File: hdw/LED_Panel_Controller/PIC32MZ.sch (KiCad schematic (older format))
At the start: 3 parts

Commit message: lots of schematic progress
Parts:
- removed U?: PIC32MZ0512EFE064T-I_PT, Package_QFP:TQFP-64_10x10mm_P0.5mm, symbol Custom_Library:PIC32MZ0512EFE064T-I_PT
- added U?: PIC32MZ2048EFG100_IPF, Housings_QFP:TQFP-100_14x14mm_Pitch0.5mm, symbol Custom_Library:PIC32MZ2048EFG100_IPF
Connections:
- net labels added: FLASH_SPI_MISO, FLASH_SPI_MOSI, FLASH_SPI_SCK, SD_CARD_DET, SD_SPI_CS, SD_SPI_MISO, SD_SPI_MOSI, SD_SPI_SCK, WIFI_CHIP_EN, WIFI_IRQN, WIFI_SPI_MISO, WIFI_SPI_MOSI, WIFI_SPI_SCK, WIFI_WAKE, ~FLASH_SPI_CE1, ~WIFI_RESET, ~WIFI_SPI_SS
- net labels removed: PIC32MZ_POSC_EC_Enable
- wire segments 33 -> 41
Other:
- note added: "I2C5"
- note added: "ICSP2"
- note added: "POSC"
- note added: "REFCLK1"
- note added: "SOSC"
- moved on the sheet: R?

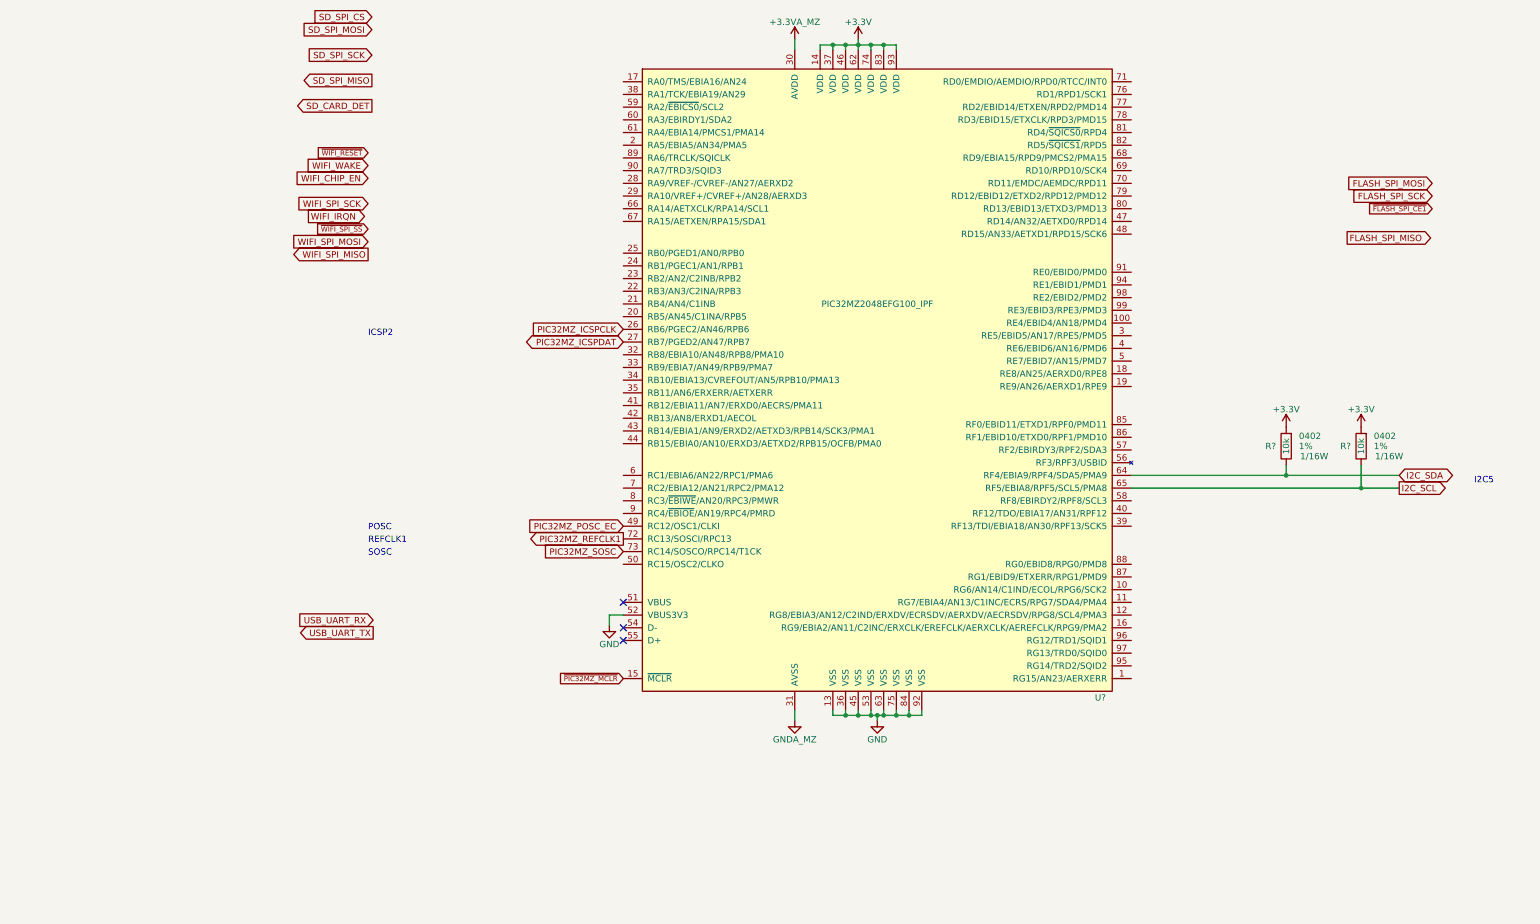
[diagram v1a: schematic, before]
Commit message: lots of MCU pin assignments
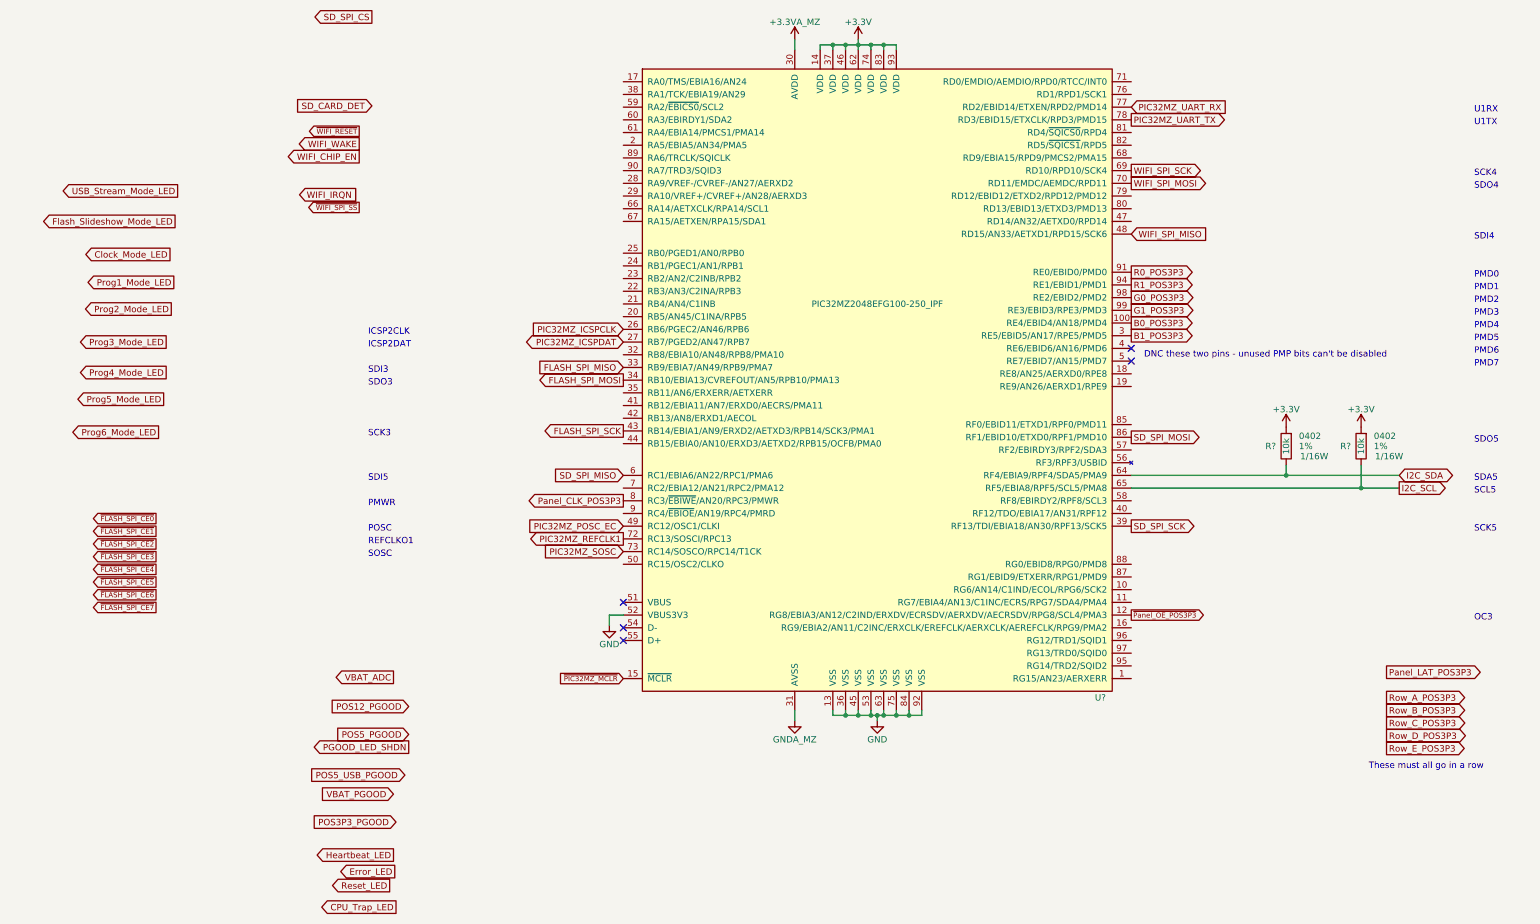
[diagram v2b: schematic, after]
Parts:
- U?: value PIC32MZ2048EFG100_IPF -> PIC32MZ2048EFG100-250_IPF; Digi-Key PN PIC32MZ2048EFG100-I/PF-ND -> PIC32MZ2048EFH100-250I/PF-ND
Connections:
- net FLASH_SPI_MISO: now also U?.33 (RB9/EBIA7/AN49/RPB9/PMA7)
- net FLASH_SPI_MOSI: now also U?.34 (RB10/EBIA13/CVREFOUT/AN5/RPB10/PMA13)
- net FLASH_SPI_SCK: now also U?.43 (RB14/EBIA1/AN9/ERXD2/AETXD3/RPB14/SCK3/PMA1)
- net SD_SPI_MISO: now also U?.6 (RC1/EBIA6/AN22/RPC1/PMA6)
- net SD_SPI_MOSI: now also U?.86 (RF1/EBID10/ETXD0/RPF1/PMD10)
- net SD_SPI_SCK: now also U?.39 (RF13/TDI/EBIA18/AN30/RPF13/SCK5)
- net WIFI_SPI_MISO: now also U?.48 (RD15/AN33/AETXD1/RPD15/SCK6)
- net WIFI_SPI_MOSI: now also U?.70 (RD11/EMDC/AEMDC/RPD11)
- net WIFI_SPI_SCK: now also U?.69 (RD10/RPD10/SCK4)
- net B0_POS3P3: now reaches U?.100 (RE4/EBID4/AN18/PMD4)
- net ~Panel_OE_POS3P3: now reaches U?.12 (RG8/EBIA3/AN12/C2IND/ERXDV/ECRSDV/AERXDV/AECRSDV/RPG8/SCL4/PMA3)
- net B1_POS3P3: now reaches U?.3 (RE5/EBID5/AN17/RPE5/PMD5)
- net PIC32MZ_UART_RX: now reaches U?.77 (RD2/EBID14/ETXEN/RPD2/PMD14)
- net PIC32MZ_UART_TX: now reaches U?.78 (RD3/EBID15/ETXCLK/RPD3/PMD15)
- net Panel_CLK_POS3P3: now reaches U?.8 (RC3/~EBIWE~/AN20/RPC3/PMWR)
- net R0_POS3P3: now reaches U?.91 (RE0/EBID0/PMD0)
- net R1_POS3P3: now reaches U?.94 (RE1/EBID1/PMD1)
- net G0_POS3P3: now reaches U?.98 (RE2/EBID2/PMD2)
- net G1_POS3P3: now reaches U?.99 (RE3/EBID3/RPE3/PMD3)
- no-connect marks 3 -> 5
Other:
- note added: "DNC these two pins - unused PMP bits can't be disabled"
- note added: "ICSP2CLK"
- note added: "ICSP2DAT"
- note added: "OC3"
- note added: "PMD0"
- note added: "PMD1"
- note added: "PMD2"
- note added: "PMD3"
- note added: "PMD4"
- note added: "PMD5"
- note added: "PMD6"
- note added: "PMD7"
- note added: "PMWR"
- note added: "REFCLKO1"
- note added: "SCK3"
- note added: "SCK4"
- note added: "SCK5"
- note added: "SCL5"
- note added: "SDA5"
- note added: "SDI3"
- note added: "SDI4"
- note added: "SDI5"
- note added: "SDO3"
- note added: "SDO4"
- note added: "SDO5"
- note added: "These must all go in a row"
- note added: "U1RX"
- note added: "U1TX"
- note removed: "I2C5"
- note removed: "ICSP2"
- note removed: "REFCLK1"
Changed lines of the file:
@@
 Text GLabel 3300 4890 0    50   Output ~ 0
 PIC32MZ_REFCLK1
-Text GLabel 1330 5630 0    50   Output ~ 0
-USB_UART_TX
-Text GLabel 1330 5530 0    50   Input ~ 0
-USB_UART_RX
+Text GLabel 7300 1590 2    50   Output ~ 0
+PIC32MZ_UART_TX
+Text GLabel 7300 1490 2    50   Input ~ 0
+PIC32MZ_UART_RX
 Text GLabel 3300 3240 0    50   Input ~ 0
 PIC32MZ_ICSPCLK
@@
 Text GLabel 3300 4990 0    50   Input ~ 0
 PIC32MZ_SOSC
-Text GLabel 1290 1850 0    40   Input ~ 0
+Text GLabel 1220 1680 0    40   Output ~ 0
 ~WIFI_RESET
-Text GLabel 1290 1950 0    50   Input ~ 0
+Text GLabel 1220 1780 0    50   Output ~ 0
 WIFI_WAKE
-Text GLabel 1290 2050 0    50   Input ~ 0
+Text GLabel 1220 1880 0    50   Output ~ 0
 WIFI_CHIP_EN
-Text GLabel 1290 2250 0    50   Input ~ 0
+Text GLabel 7300 1990 2    50   Output ~ 0
 WIFI_SPI_SCK
-Text GLabel 1290 2450 0    40   Input ~ 0
+Text GLabel 1220 2280 0    40   Output ~ 0
 ~WIFI_SPI_SS
-Text GLabel 1290 2550 0    50   Input ~ 0
+Text GLabel 7300 2090 2    50   Output ~ 0
 WIFI_SPI_MOSI
-Text GLabel 1290 2650 0    50   Output ~ 0
+Text GLabel 7300 2490 2    50   Input ~ 0
 WIFI_SPI_MISO
-Text GLabel 820  2350 2    50   Output ~ 0
+Text GLabel 750  2180 2    50   Input ~ 0
 WIFI_IRQN
 $Comp
@@
 P 5300 3640
 F 0 "U?" H 7100 1140 50  0000 R CNN
-F 1 "PIC32MZ2048EFG100_IPF" H 5300 4240 50  0000 C CNN
+F 1 "PIC32MZ2048EFG100-250_IPF" H 5300 4240 50  0000 C CNN
 F 2 "Housings_QFP:TQFP-100_14x14mm_Pitch0.5mm" H 5300 3640 50  0001 C CNN
 F 3 "http://ww1.microchip.com/downloads/en/DeviceDoc/60001320E.pdf" H 5300 3640 50  0001 C CNN
-F 4 "PIC32MZ2048EFG100-I/PF-ND" H 5300 3640 50  0001 C CNN "Digi-Key PN"
+F 4 "PIC32MZ2048EFH100-250I/PF-ND" H 5300 3640 50  0001 C CNN "Digi-Key PN"
 	1    5300 3640
 	1    0    0    -1
@@
 	1    0    0    -1
 $EndComp
-Text Notes 10000 4460 0    50   ~ 0
-I2C5
-Text Notes 1290 3300 0    50   ~ 0
-ICSP2
-Text Notes 1290 4830 0    50   ~ 0
+Text Notes 10000 4440 0    50   ~ 0
+SDA5
+Text Notes 1290 3290 0    50   ~ 0
+ICSP2CLK
+Text Notes 1290 4840 0    50   ~ 0
 POSC
-Text Notes 1290 4930 0    50   ~ 0
-REFCLK1
-Text Notes 1290 5030 0    50   ~ 0
+Text Notes 1290 4940 0    50   ~ 0
+REFCLKO1
+Text Notes 1290 5040 0    50   ~ 0
 SOSC
-Text GLabel 1320 780  0    50   Input ~ 0
+Text GLabel 1320 780  0    50   Output ~ 0
 SD_SPI_CS
-Text GLabel 1320 880  0    50   Input ~ 0
+Text GLabel 7300 4090 2    50   Output ~ 0
 SD_SPI_MOSI
-Text GLabel 1320 1080 0    50   Input ~ 0
+Text GLabel 7300 4790 2    50   Output ~ 0
 SD_SPI_SCK
-Text GLabel 1320 1280 0    50   Output ~ 0
+Text GLabel 3300 4390 0    50   Input ~ 0
 SD_SPI_MISO
-Text GLabel 1320 1480 0    50   Output ~ 0
+Text GLabel 1320 1480 0    50   Input ~ 0
 SD_CARD_DET
-Text GLabel 9670 2190 0    50   Input ~ 0
+Text GLabel 3300 4040 0    50   Output ~ 0
 FLASH_SPI_SCK
-Text GLabel 9670 2290 0    40   Input ~ 0
+Text GLabel 3300 3640 0    50   Output ~ 0
+FLASH_SPI_MOSI
+Text GLabel 3300 3540 0    50   Input ~ 0
+FLASH_SPI_MISO
+Text Notes 10000 1540 0    50   ~ 0
+U1RX
+Text Notes 10000 1640 0    50   ~ 0
+U1TX
+Text GLabel 7300 3090 2    50   Output ~ 0
+G1_POS3P3
+Text GLabel 7300 2990 2    50   Output ~ 0
+G0_POS3P3
+Text GLabel 7300 3290 2    50   Output ~ 0
+B1_POS3P3
+Text GLabel 7300 2890 2    50   Output ~ 0
+R1_POS3P3
+Text GLabel 7300 3190 2    50   Output ~ 0
+B0_POS3P3
+Text GLabel 7300 2790 2    50   Output ~ 0
+R0_POS3P3
+Text Notes 10000 2840 0    50   ~ 0
+PMD0
+Text Notes 10000 2940 0    50   ~ 0
+PMD1
+Text Notes 10000 3040 0    50   ~ 0
+PMD2
+Text Notes 10000 3140 0    50   ~ 0
+PMD3
+Text Notes 10000 3240 0    50   ~ 0
+PMD4
+Text Notes 10000 3340 0    50   ~ 0
+PMD5
+Text GLabel 9310 5940 2    50   Output ~ 0
+Panel_LAT_POS3P3
+Text GLabel 7300 5490 2    40   Output ~ 0
+~Panel_OE_POS3P3
+Text GLabel 3300 4590 0    50   Output ~ 0
+Panel_CLK_POS3P3
+Text GLabel 9310 6340 2    50   Output ~ 0
+Row_C_POS3P3
+Text GLabel 9310 6540 2    50   Output ~ 0
+Row_E_POS3P3
+Text GLabel 9310 6440 2    50   Output ~ 0
+Row_D_POS3P3
+Text GLabel 9310 6240 2    50   Output ~ 0
+Row_B_POS3P3
+Text GLabel 9310 6140 2    50   Output ~ 0
+Row_A_POS3P3
+Text Notes 1290 4640 0    50   ~ 0
+PMWR
+Text Notes 1290 3390 0    50   ~ 0
+ICSP2DAT
+Text Notes 10000 4540 0    50   ~ 0
+SCL5
+Text Notes 10000 3540 0    50   ~ 0
+PMD7
+Text Notes 10000 3440 0    50   ~ 0
+PMD6
+NoConn ~ 7300 3490
+NoConn ~ 7300 3390
+Text Notes 7400 3470 0    50   ~ 0
+DNC these two pins - unused PMP bits can't be disabled
+Text Notes 10000 5540 0    50   ~ 0
+OC3
+Text Notes 9170 6710 0    50   ~ 0
+These must all go in a row
+Text Notes 1290 4090 0    50   ~ 0
+SCK3
+Text Notes 1290 3690 0    50   ~ 0
+SDO3
+Text Notes 1290 3590 0    50   ~ 0
+SDI3
+Text Notes 10000 2040 0    50   ~ 0
+SCK4
+Text Notes 10000 2140 0    50   ~ 0
+SDO4
+Text Notes 10000 2540 0    50   ~ 0
+SDI4
+Text Notes 10000 4840 0    50   ~ 0
+SCK5
+Text Notes 1290 4440 0    50   ~ 0
+SDI5
+Text Notes 10000 4140 0    50   ~ 0
+SDO5
+Text GLabel 1610 6210 0    50   Input ~ 0
+POS12_PGOOD
+Text GLabel 1610 6430 0    50   Input ~ 0
+POS5_PGOOD
+Text GLabel 1610 6530 0    50   Output ~ 0
+PGOOD_LED_SHDN
+Text GLabel 1510 7120 0    50   Input ~ 0
+POS3P3_PGOOD
+Text GLabel 1490 6900 0    50   Input ~ 0
+VBAT_PGOOD
+Text GLabel 1580 6750 0    50   Input ~ 0
+POS5_USB_PGOOD
+Text GLabel 1490 7380 0    50   Output ~ 0
+Heartbeat_LED
+Text GLabel 1460 7620 0    50   Output ~ 0
+Reset_LED
+Text GLabel 1500 7510 0    50   Output ~ 0
+Error_LED
+Text GLabel 1510 7790 0    50   Output ~ 0
+CPU_Trap_LED
+Text GLabel 1490 5980 0    50   Output ~ 0
+VBAT_ADC
+Text GLabel -210 2150 0    50   Output ~ 0
+USB_Stream_Mode_LED
+Text GLabel -240 2870 0    50   Output ~ 0
+Prog1_Mode_LED
+Text GLabel -300 3580 0    50   Output ~ 0
+Prog4_Mode_LED
+Text GLabel -230 2390 0    50   Output ~ 0
+Flash_Slideshow_Mode_LED
+Text GLabel -260 3080 0    50   Output ~ 0
+Prog2_Mode_LED
+Text GLabel -320 3790 0    50   Output ~ 0
+Prog5_Mode_LED
+Text GLabel -300 3340 0    50   Output ~ 0
+Prog3_Mode_LED
+Text GLabel -360 4050 0    50   Output ~ 0
+Prog6_Mode_LED
+Text GLabel -270 2650 0    50   Output ~ 0
+Clock_Mode_LED
+Text GLabel -380 4730 0    40   Output ~ 0
+~FLASH_SPI_CE0
+Text GLabel -380 4830 0    40   Output ~ 0
 ~FLASH_SPI_CE1
-Text GLabel 9670 2090 0    50   Input ~ 0
-FLASH_SPI_MOSI
-Text GLabel 9000 2520 2    50   Output ~ 0
-FLASH_SPI_MISO
+Text GLabel -380 4930 0    40   Output ~ 0
+~FLASH_SPI_CE2
+Text GLabel -380 5030 0    40   Output ~ 0
+~FLASH_SPI_CE3
+Text GLabel -380 5130 0    40   Output ~ 0
+~FLASH_SPI_CE4
+Text GLabel -380 5230 0    40   Output ~ 0
+~FLASH_SPI_CE5
+Text GLabel -380 5330 0    40   Output ~ 0
+~FLASH_SPI_CE6
+Text GLabel -380 5430 0    40   Output ~ 0
+~FLASH_SPI_CE7
 $EndSCHEMATC
